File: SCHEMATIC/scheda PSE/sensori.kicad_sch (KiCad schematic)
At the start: 15 parts

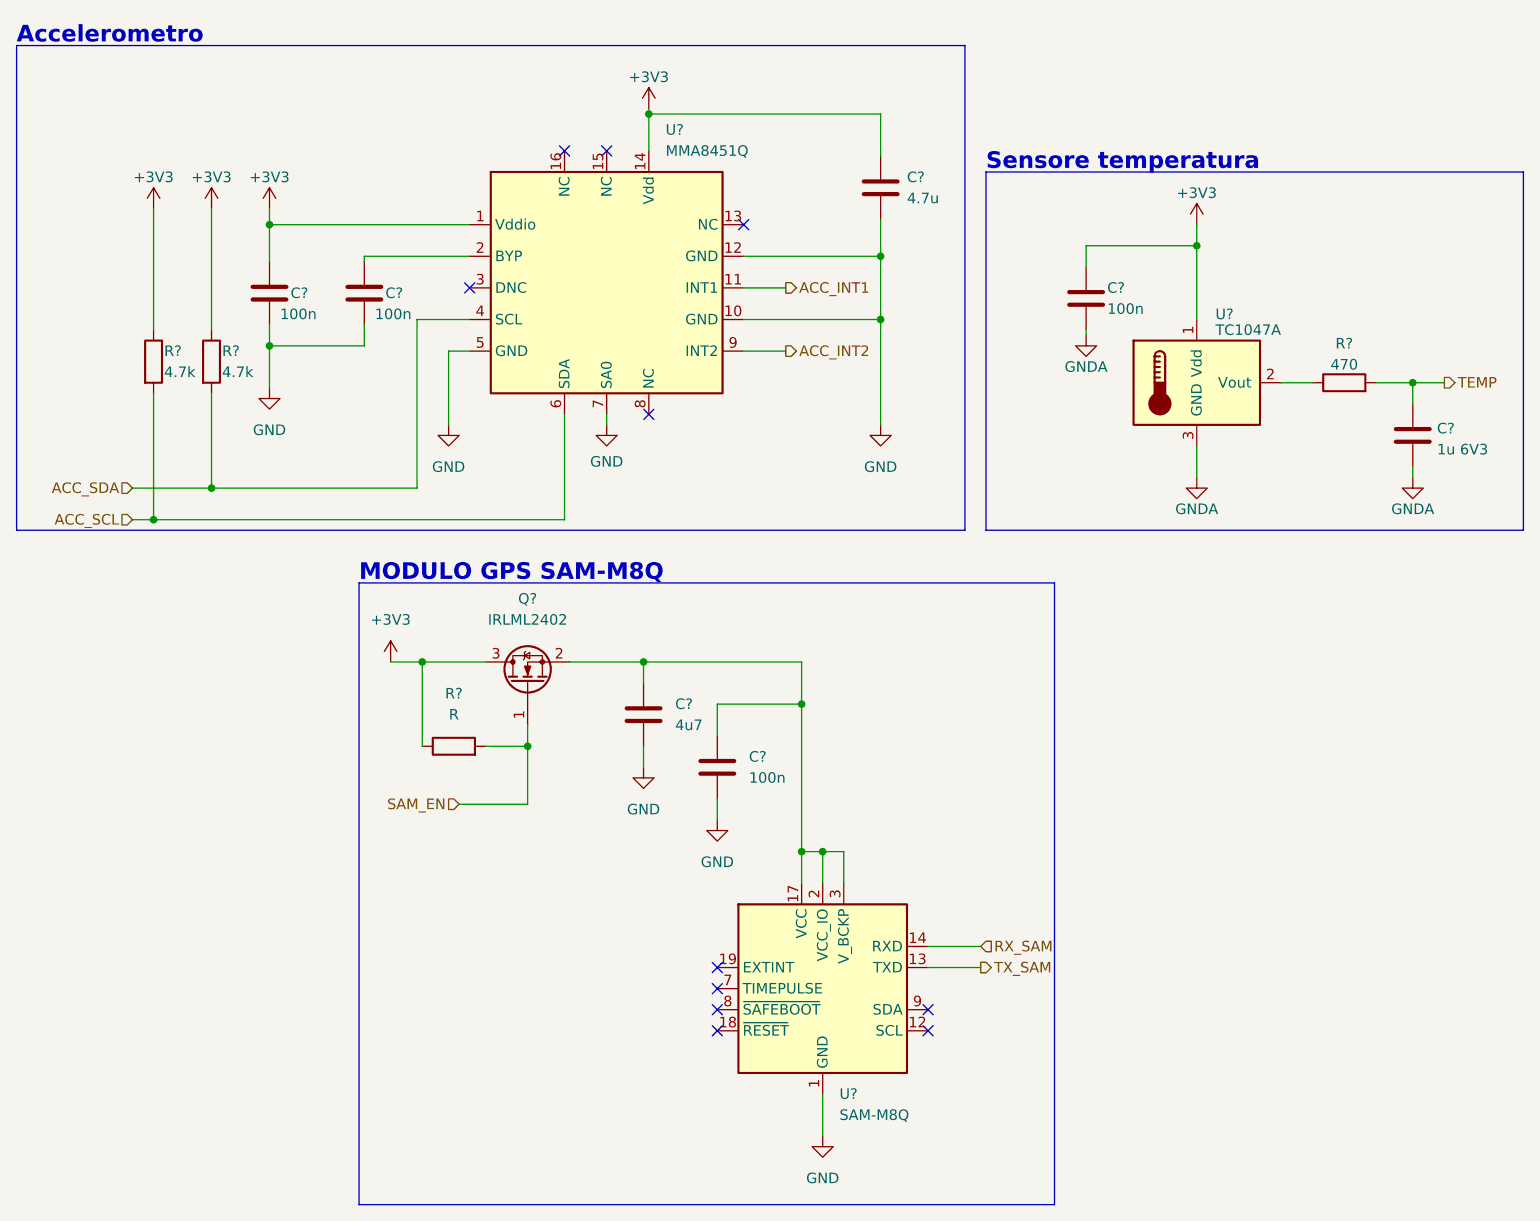
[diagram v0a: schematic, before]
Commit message: sistemato tutto, e aggiunti i footprint da modificare
sistemato tutto, aggiunto e modificato i footprint.
Manca solo aggiungere i restanti footprint (praticamente solo dei componenti comuni)
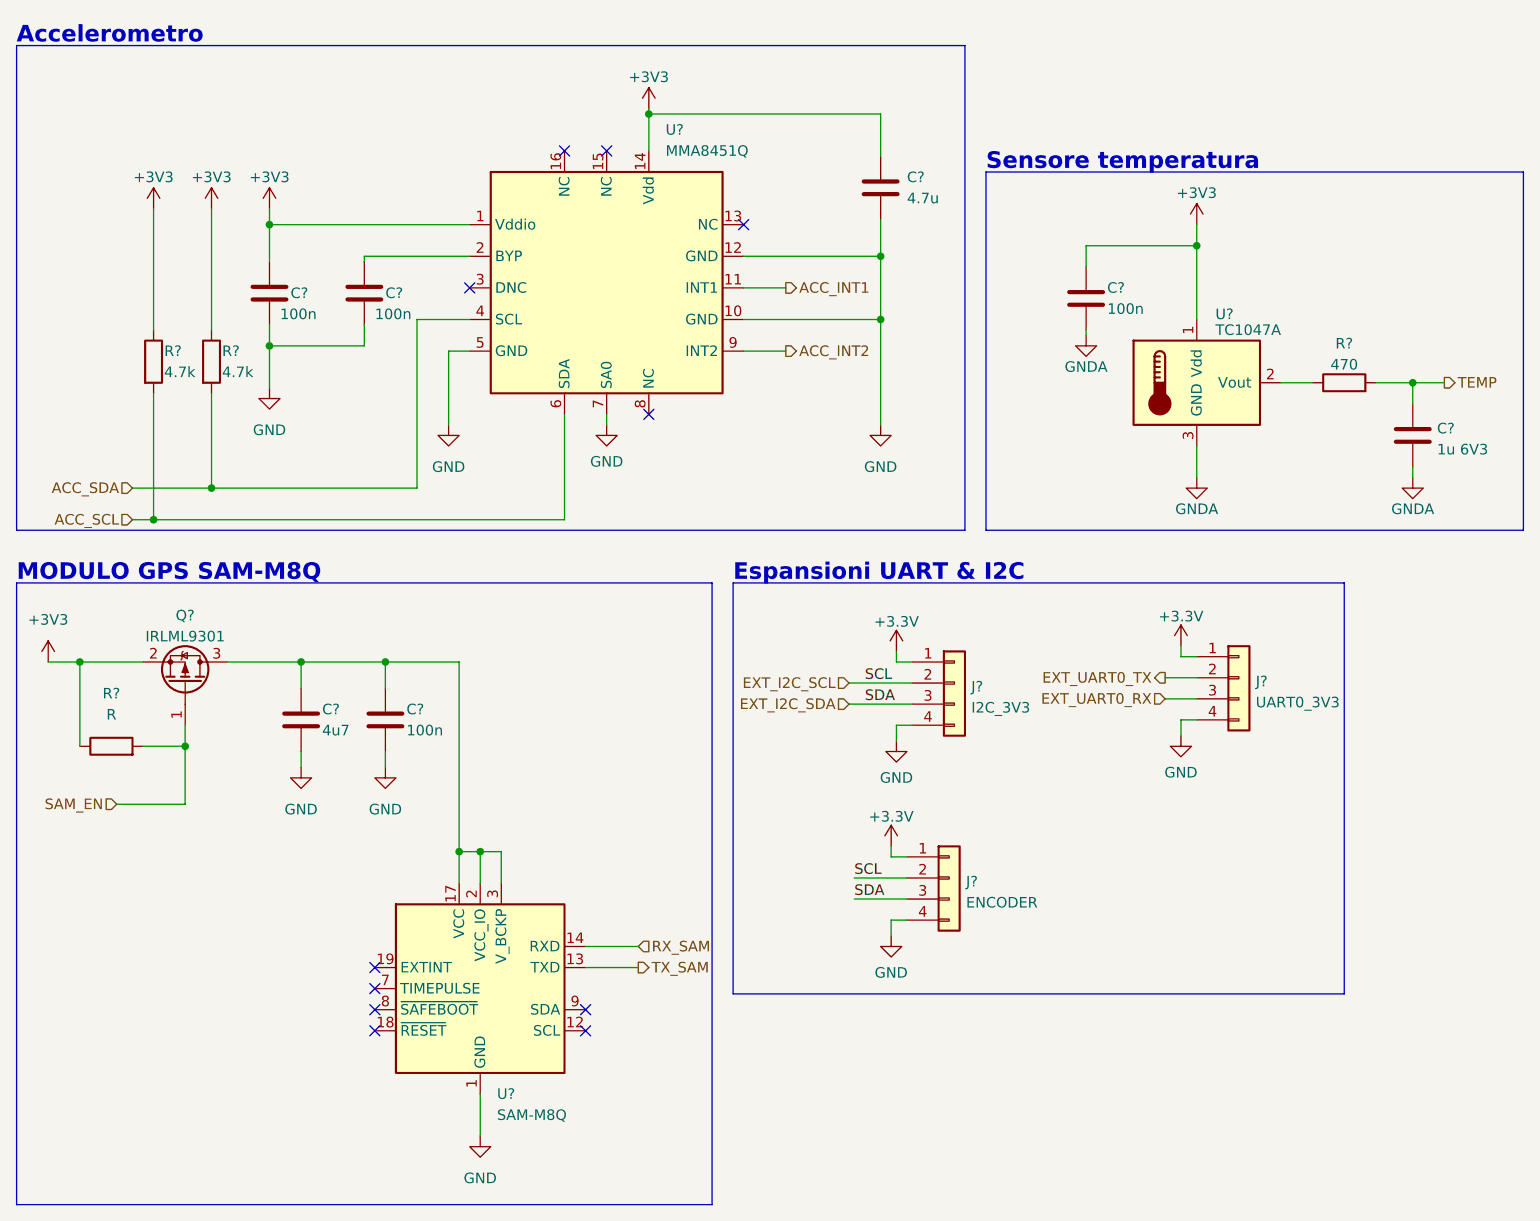
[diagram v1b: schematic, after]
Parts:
- removed Q?: IRLML2402, Package_TO_SOT_SMD:SOT-23, symbol Transistor_FET:IRLML2060
- added J?: UART0_3V3, symbol Connector_Generic:Conn_01x04
- added J?: I2C_3V3, symbol Connector_Generic:Conn_01x04
- added J?: ENCODER, symbol Connector_Generic:Conn_01x04
- added Q?: IRLML9301, Package_TO_SOT_SMD:SOT-23, symbol Transistor_FET:IRLML9301
- U?: footprint RF_GPS:ublox_SAM-M8Q -> _PSE:SAM_M8Q
- U?: footprint (none) -> _PSE:QFN-16
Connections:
- net +3V3: now also Q?.2 (S)
- net GND: now also J?.4 (Pin_4), J?.4 (Pin_4), J?.4 (Pin_4)
- net SAM_EN: now also Q?.1 (G)
- net at C?.1, C?.1, U?.17 (VCC)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: now also Q?.3 (D)
- new net +3.3V: J?.1 (Pin_1), J?.1 (Pin_1), J?.1 (Pin_1)
- new net EXT_I2C_SCL: J?.2 (Pin_2), J?.2 (Pin_2)
- new net EXT_I2C_SDA: J?.3 (Pin_3), J?.3 (Pin_3)
- new net EXT_UART0_RX: J?.3 (Pin_3)
- new net EXT_UART0_TX: J?.2 (Pin_2)
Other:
- note added: "Espansioni UART & I2C"
- moved on the sheet: C?, R?, U?

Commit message: Aggiunti QUASI tutti i footprint
aggiunti quasi tutti i footprint dei componenti
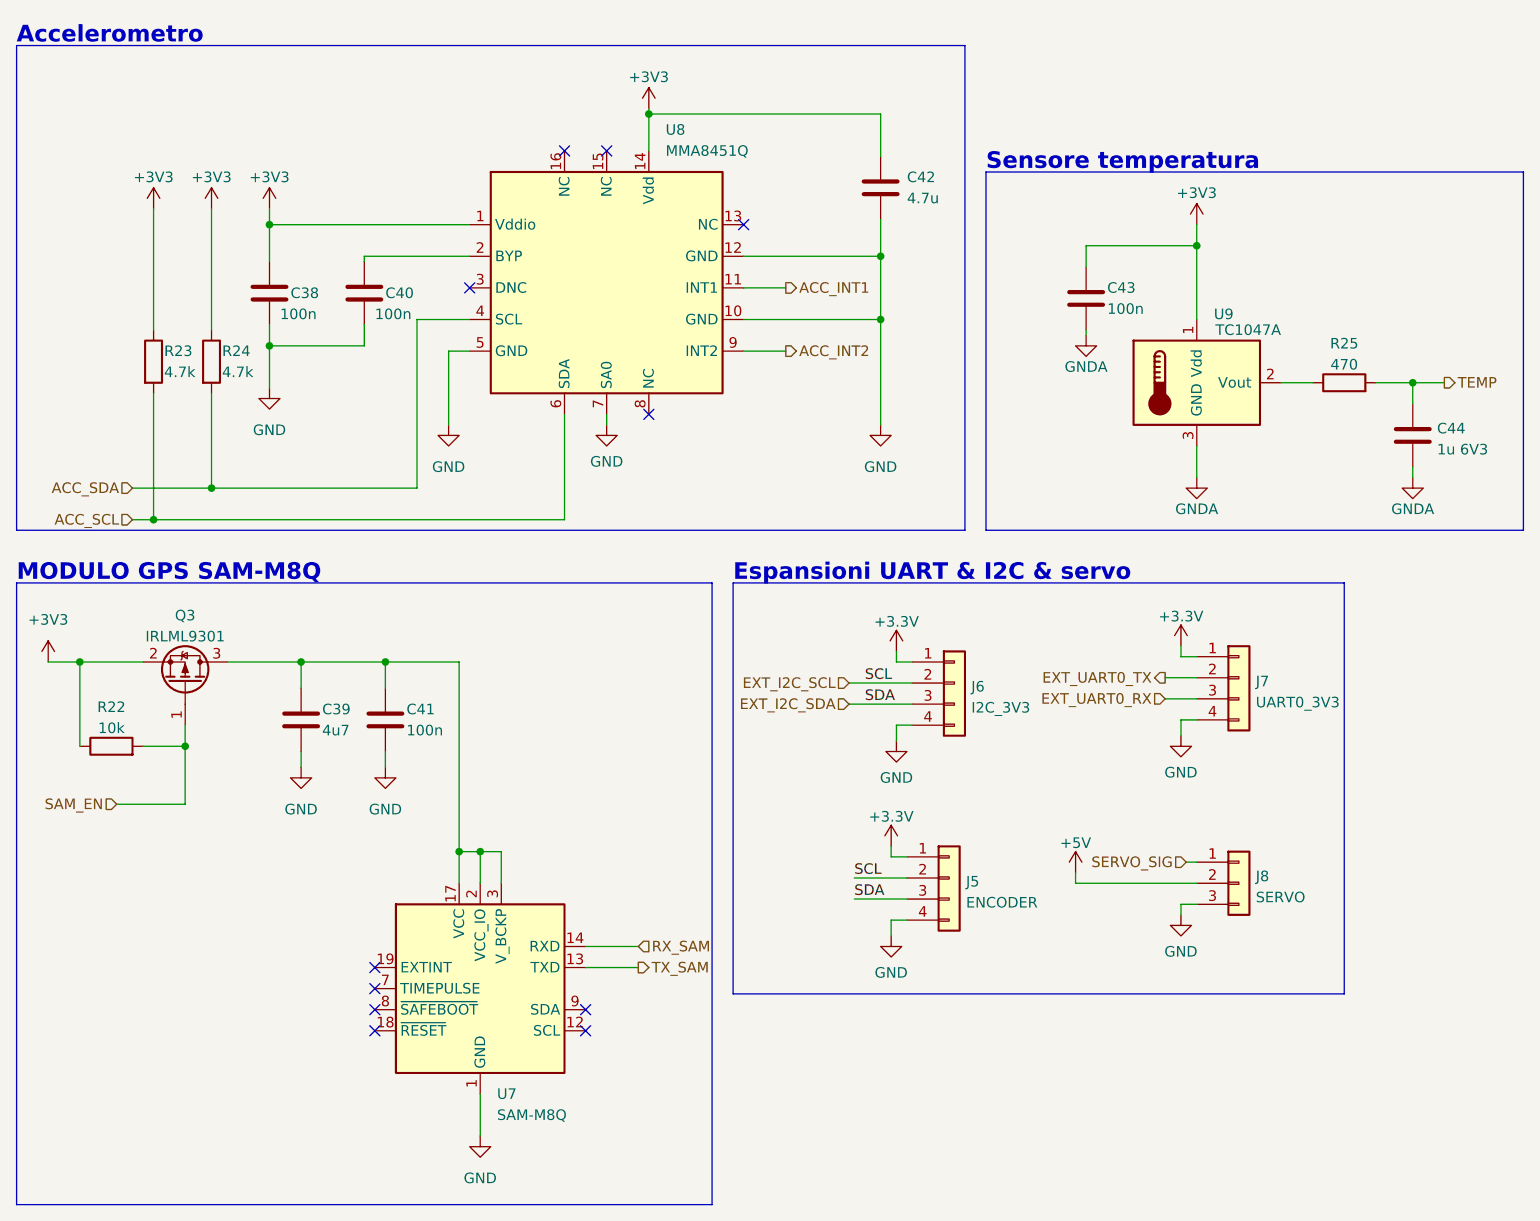
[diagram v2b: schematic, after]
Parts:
- added J8: SERVO, Connector_PinSocket_2.54mm:PinSocket_1x03_P2.54mm_Vertical, symbol Connector_Generic:Conn_01x03
- C38, C39, C40, C41, C42, C43, C44: renamed from C?; footprint (none) -> Capacitor_SMD:C_0603_1608Metric
- J6, J7: renamed from J?; footprint (none) -> Connector_PinSocket_2.54mm:PinSocket_1x04_P2.54mm_Vertical
- R22: renamed from R?; value R -> 10k; footprint (none) -> Resistor_SMD:R_0603_1608Metric
- R23, R24, R25: renamed from R?; footprint (none) -> Resistor_SMD:R_0603_1608Metric
- gave numbers to parts that had none: 5
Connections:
- net GND: now also J8.3 (Pin_3)
- new net +5V: J8.2 (Pin_2)
- new net SERVO_SIG: J8.1 (Pin_1)
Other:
- note added: "Espansioni UART & I2C & servo"
- note removed: "Espansioni UART & I2C"

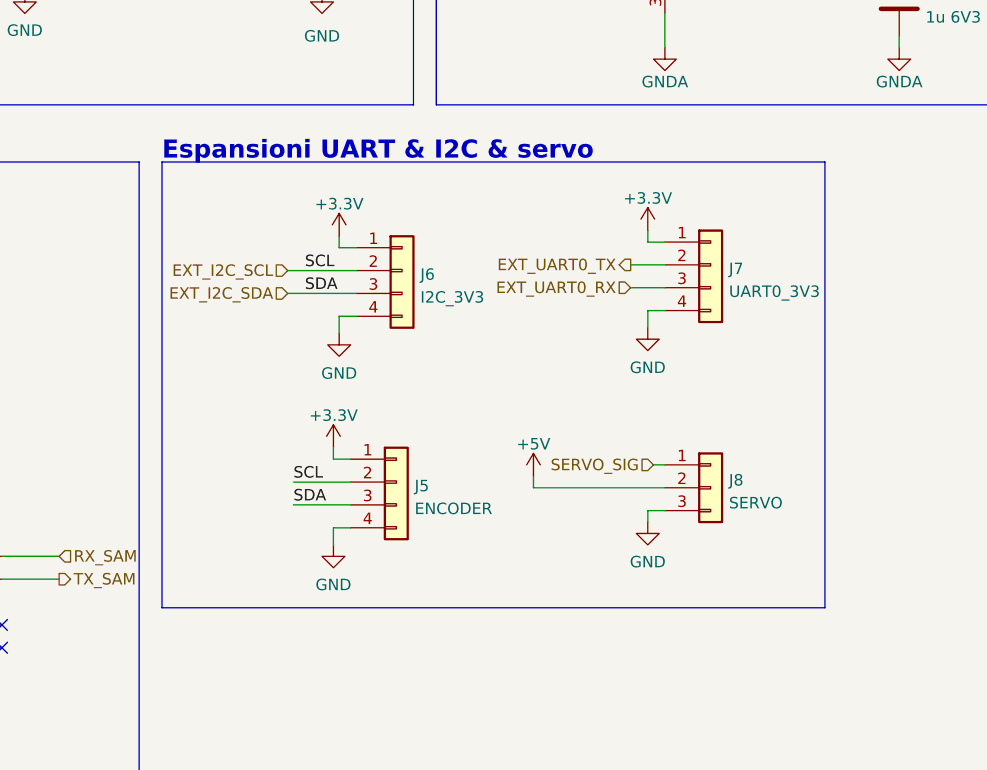
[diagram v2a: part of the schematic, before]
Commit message: iniziato il layout, posizionati componenti principali
incominciato il posizionamento dei componenti nel layout. Sono stati posizionati i componenti principali come led RGB, GPS, schermo, pulsanti vari, buzzer
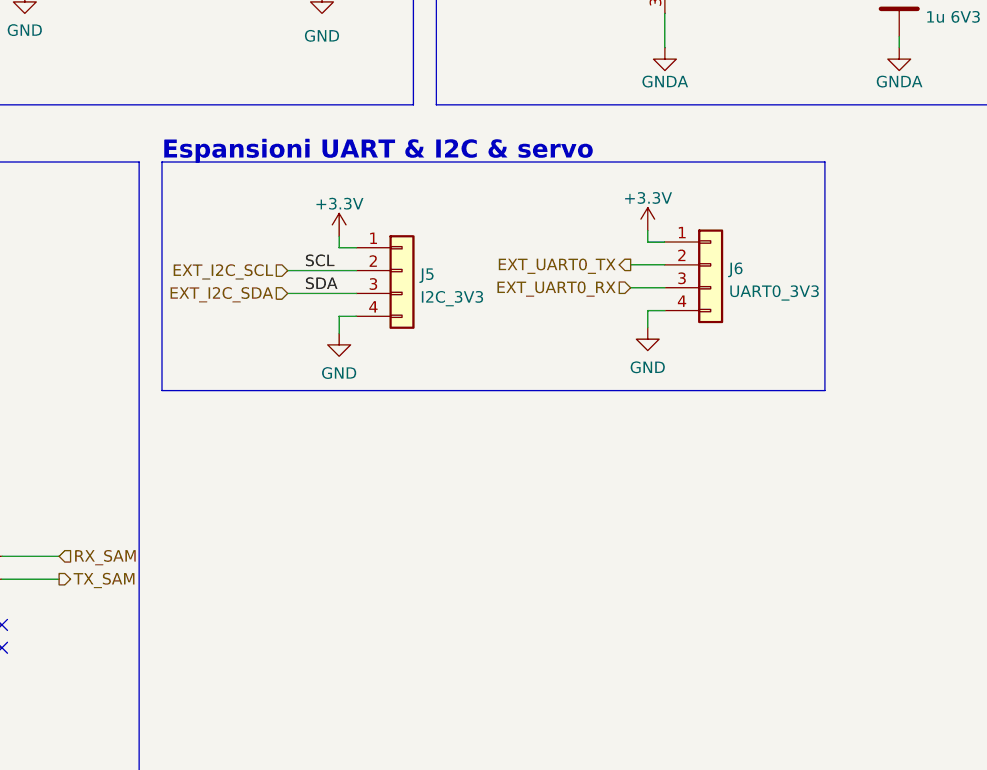
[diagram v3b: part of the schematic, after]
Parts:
- removed J5: ENCODER, symbol Connector_Generic:Conn_01x04
- removed J8: SERVO, Connector_PinSocket_2.54mm:PinSocket_1x03_P2.54mm_Vertical, symbol Connector_Generic:Conn_01x03
- J5: renamed from J6; footprint Connector_PinSocket_2.54mm:PinSocket_1x04_P2.54mm_Vertical -> Connector_JST:JST_XH_B4B-XH-A_1x04_P2.50mm_Vertical
- J6: renamed from J7; footprint Connector_PinSocket_2.54mm:PinSocket_1x04_P2.54mm_Vertical -> Connector_JST:JST_XH_B4B-XH-A_1x04_P2.50mm_Vertical
